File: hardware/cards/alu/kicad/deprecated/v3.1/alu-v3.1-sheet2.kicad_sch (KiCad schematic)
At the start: 41 parts

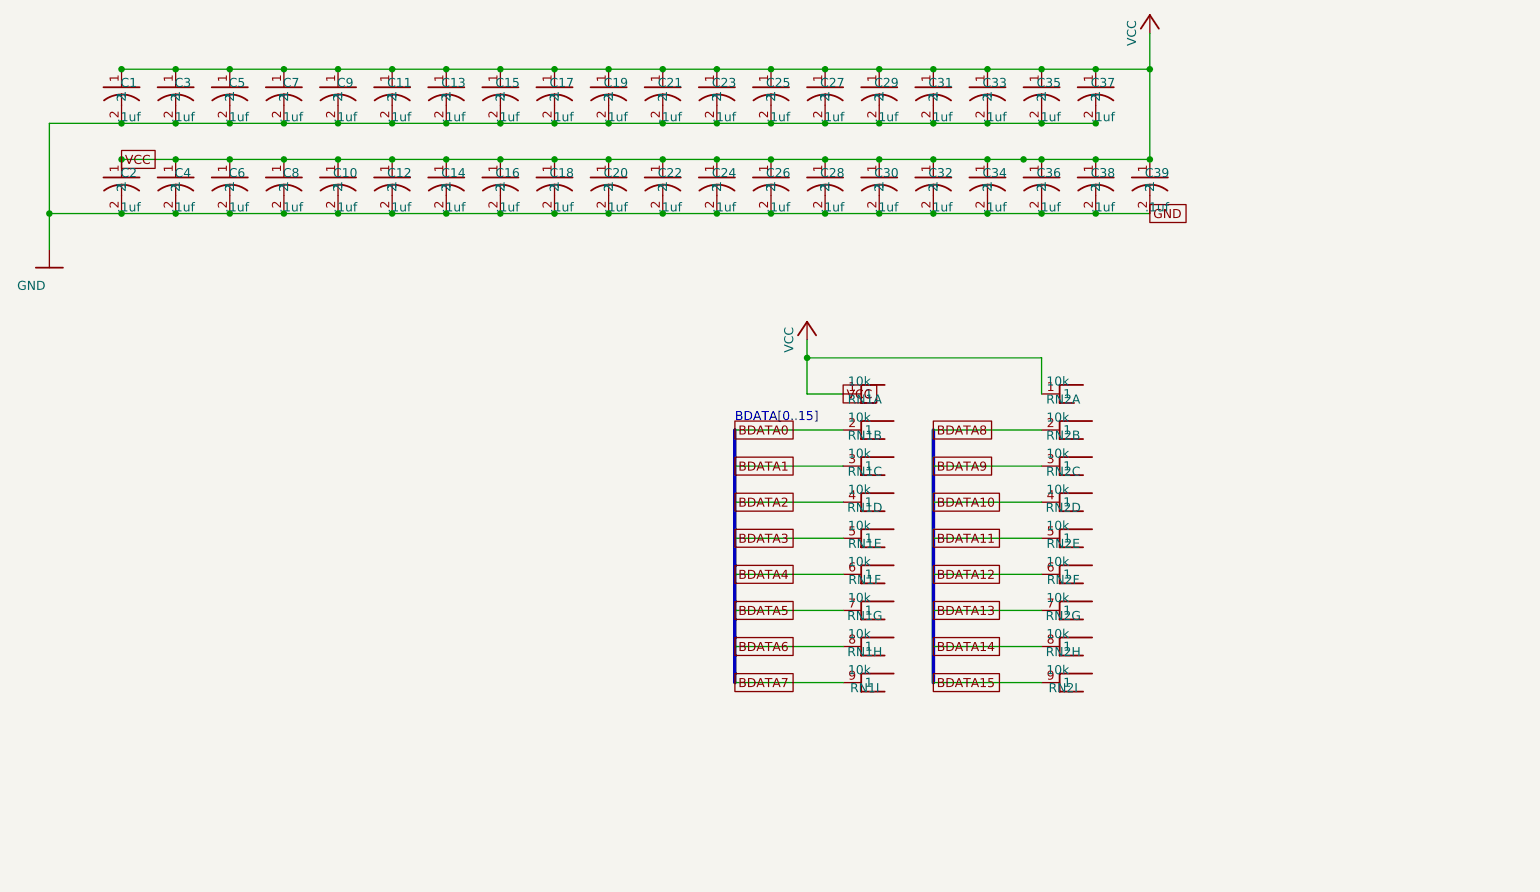
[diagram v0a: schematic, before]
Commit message: fix(kicad): readable converted schematics - overlaps 42,847 -> 3,147, nothing off the frame; CF sheet 0 overlaps
- tools/kicad/sch_overlaps.py: calibrated readability check (text/text, text/body, text/line, off frame/title block)
- eagle_sch_to_kicad.py: fields placed from Eagle's smashed attributes or the symbol's >NAME/>VALUE with Eagle's align,
  size and ratio, readable angles; fields Eagle never shows hidden (FABC96R shows only its pin name); pin numbers hidden
  where every Eagle pin hides them; Eagle-hidden layers dropped (the stray SpiceOrder text); labels on their own wires,
  converter labels only where KiCad needs them; rotate-then-mirror fixed for MR90/MR270 in pin_world/no-connects;
  each sheet on the smallest page that holds it, centred clear of the title block
- finish_board.py: stable footprint-library choice (DRC counts no longer vary run to run)
- all 37 projects regenerated: netlist proofs unchanged (34 MATCH, 2 schematic-only, video Fusion export MISMATCH as
  before); DRC same or better; ERC up (loose wire ends onto graphic buses no longer hidden by labels; explained per README)
- CF card: gate names off the gate bodies, U3 clear of its title, 5.08 mm connector pins; rebuilt: DRC 0/0, proof MATCH
- schematic PDFs regenerated (tools/sch_to_pdf.py, 37/37)

Co-Authored-By: Claude Opus 5.5 <noreply@anthropic.com>
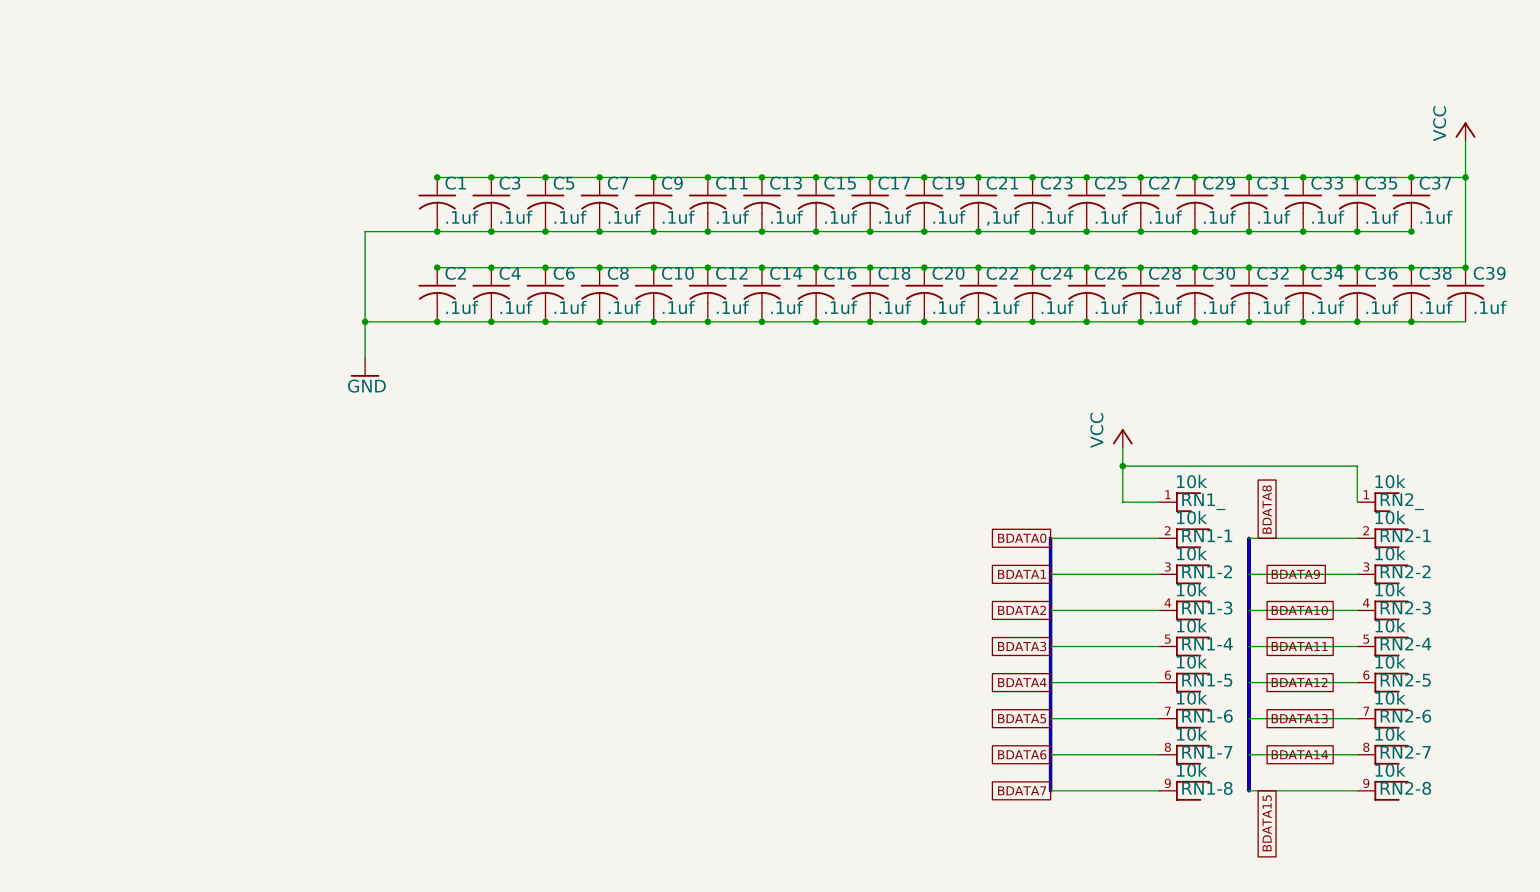
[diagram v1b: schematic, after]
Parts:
- RN1: Eagle name (none) -> RN1-3
- RN1: Eagle name (none) -> RN1_
- RN1: Eagle name (none) -> RN1-4
- RN1: Eagle name (none) -> RN1-8
- RN1: Eagle name (none) -> RN1-2
- RN1: Eagle name (none) -> RN1-6
- RN1: Eagle name (none) -> RN1-1
- RN1: Eagle name (none) -> RN1-7
- RN1: Eagle name (none) -> RN1-5
- RN2: Eagle name (none) -> RN2-6
- RN2: Eagle name (none) -> RN2-5
- RN2: Eagle name (none) -> RN2-2
- RN2: Eagle name (none) -> RN2-1
- RN2: Eagle name (none) -> RN2-3
- RN2: Eagle name (none) -> RN2-4
- RN2: Eagle name (none) -> RN2_
- RN2: Eagle name (none) -> RN2-7
- RN2: Eagle name (none) -> RN2-8
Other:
- note removed: "BDATA[0..15]"
